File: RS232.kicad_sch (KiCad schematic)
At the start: 15 parts, among them Q5 BSS84, Q6 BSS84, Q9 BSS84, U9 MAX3227

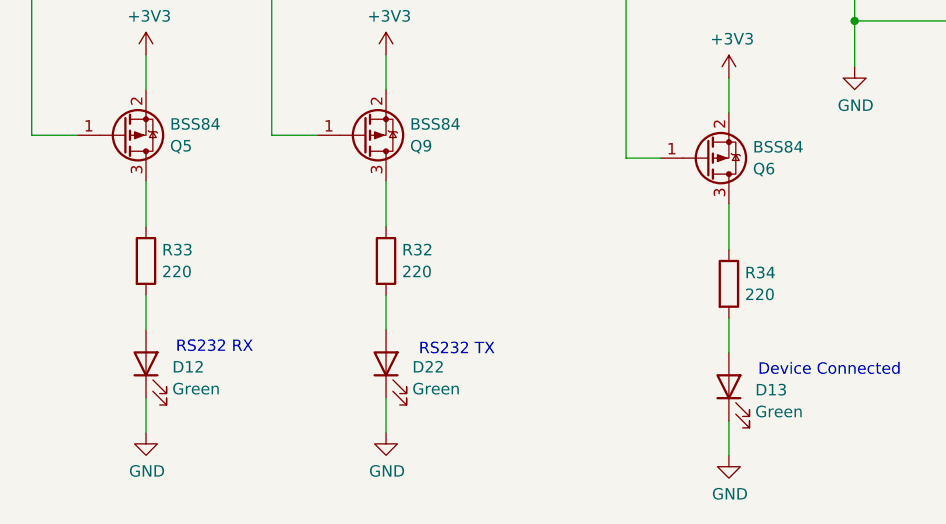
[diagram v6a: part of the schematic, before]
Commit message: update resistors to more commmon values
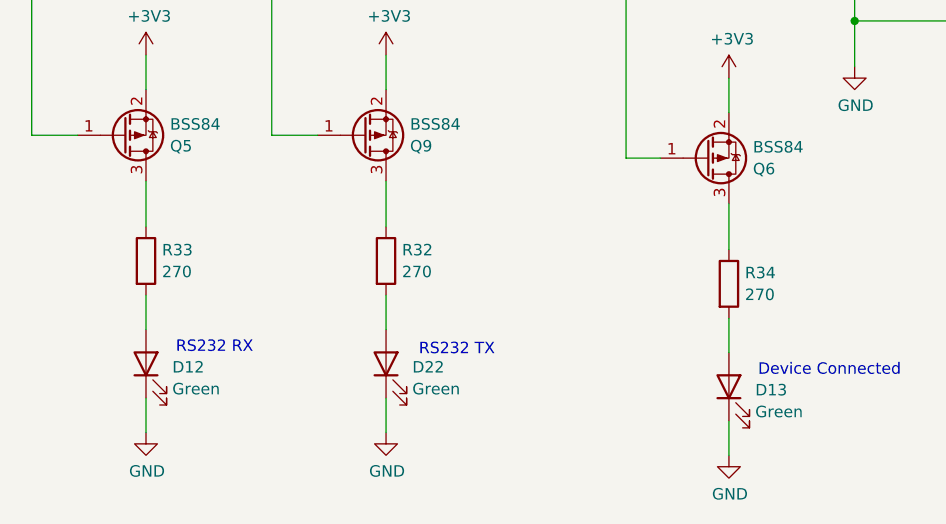
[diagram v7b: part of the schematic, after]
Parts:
- R32, R33, R34: value 220 -> 270
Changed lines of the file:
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@@
 			)
 		)
-		(property "Value" "220"
+		(property "Value" "270"
 			(at 116.078 145.9921 0)
 			(effects
@@
 			)
 		)
-		(property "Value" "220"
+		(property "Value" "270"
 			(at 51.308 143.4521 0)
 			(effects
@@
 			)
 		)
-		(property "Value" "220"
+		(property "Value" "270"
 			(at 77.978 143.4521 0)
 			(effects

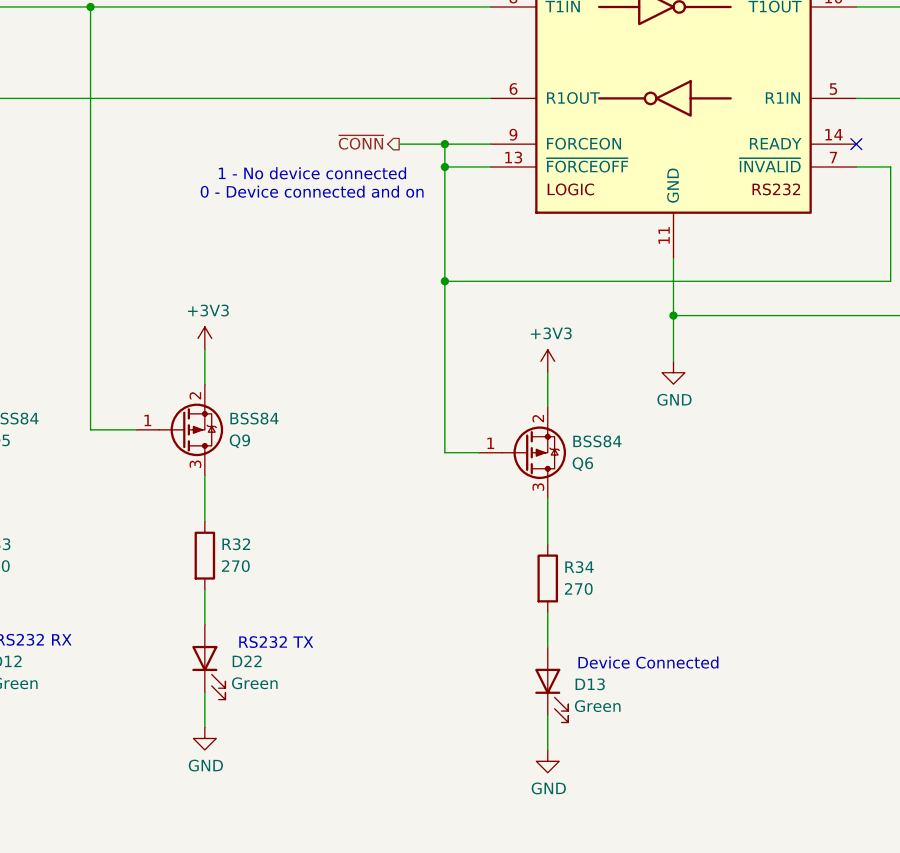
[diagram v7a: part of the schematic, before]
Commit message: flip logic on rs232 conn led
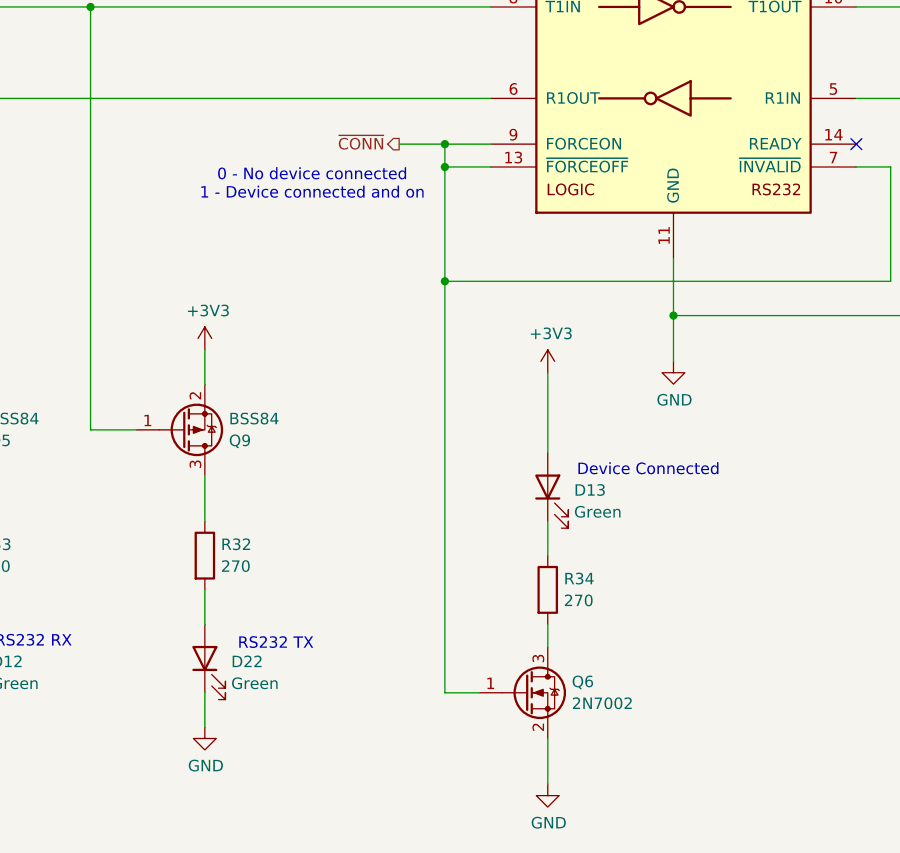
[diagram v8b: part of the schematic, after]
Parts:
- removed Q6: BSS84, Package_TO_SOT_SMD:SOT-23, symbol Transistor_FET:BSS84
- added Q6: 2N7002, Package_TO_SOT_SMD:SOT-23, symbol Transistor_FET:2N7002
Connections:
- net +3V3: now also D13.2 (A)
- net GND: now also Q6.2 (S); no longer D13.1 (K)
- net ~{CONN}: now also Q6.1 (G)
- net at R34.1: now also D13.1 (K)
- net at R34.2: now also Q6.3 (D); no longer D13.2 (A)
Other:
- note added: "0 - No device connected 1 - Device connected and on"
- note removed: "1 - No device connected 0 - Device connected and on"
- moved on the sheet: D13, R34
